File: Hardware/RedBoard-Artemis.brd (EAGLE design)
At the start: 68.6 x 58.4 mm, 115 parts, among them IC3 LM1117, J2 CORTEX_DEBUG, J3 POWER_JACKTOE, J5 USB-C, Q1 2.5A/30V/105mΩ, U1 ARTEMIS_MODULESMD, U3 AP2112-3.3V, U5 CH340C, Y1 32.768kHz

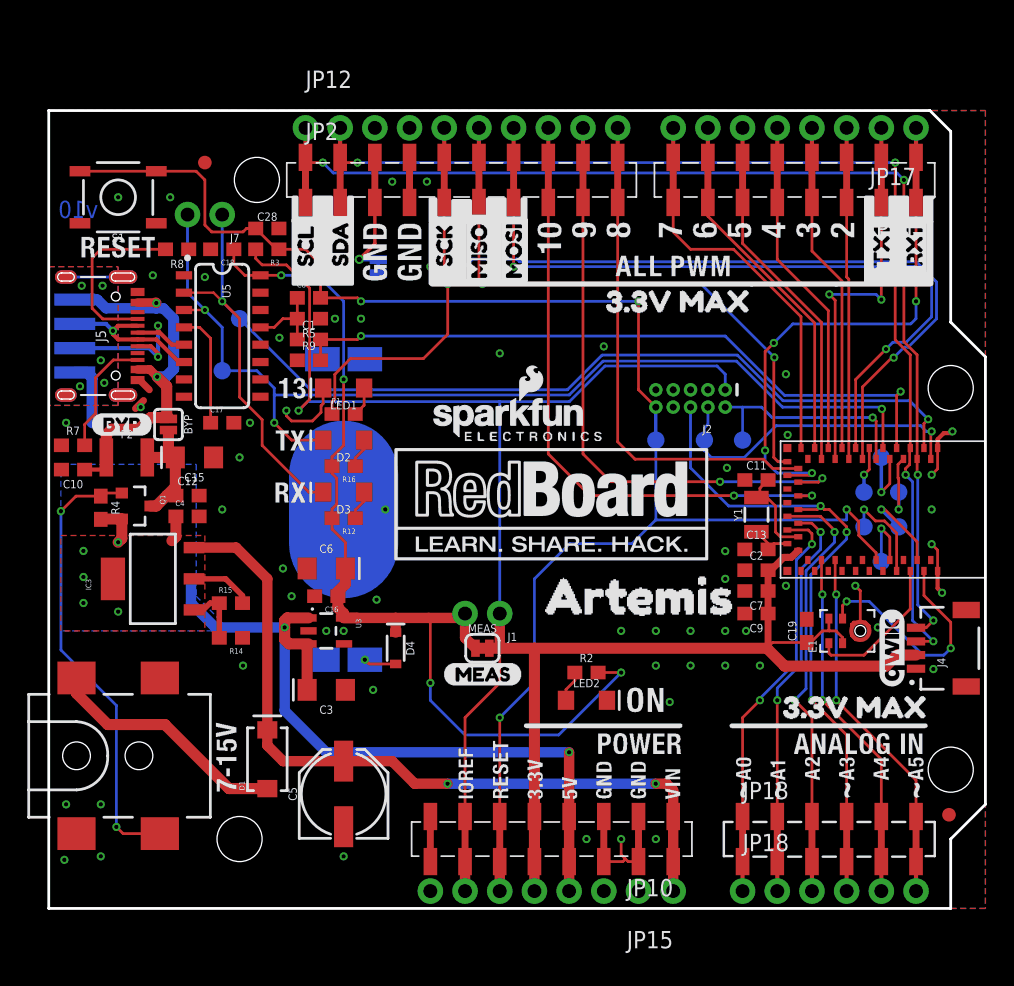
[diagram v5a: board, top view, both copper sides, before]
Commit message: Add bottom silk indicators. Move MEAS jumper.
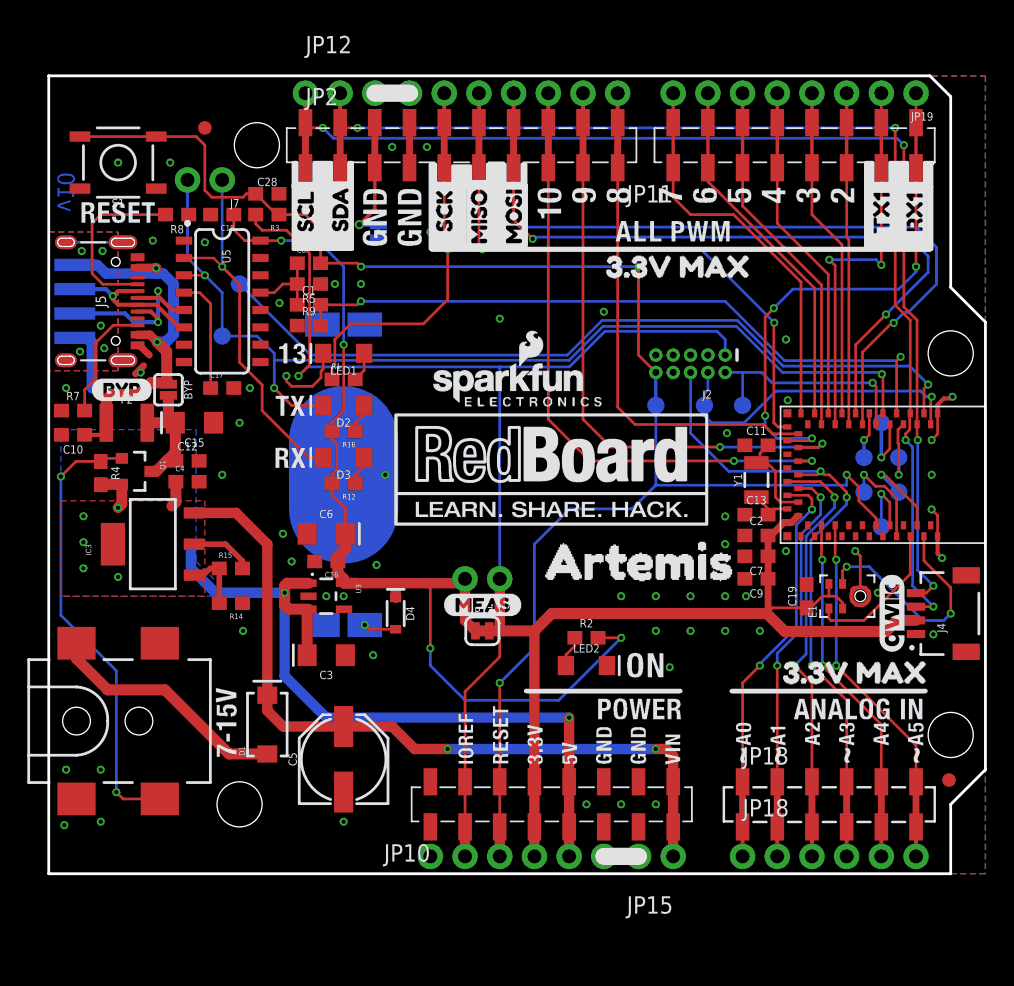
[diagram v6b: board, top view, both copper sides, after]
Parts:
- removed FRAME1: FRAME-LETTER, SparkFun-Aesthetics:CREATIVE_COMMONS
- removed MEAS: (no value), SparkFun-Jumpers:SMT-JUMPER_2_NC_TRACE_SILK
- added FRAME3: FRAME-LEDGER, SparkFun-Aesthetics:CREATIVE_COMMONS
- added JP19: (no value), SparkFun-Connectors:1X08_NO_SILK
- added U$1: (no value), buzzard_labels (6):SCL1
- added U$26: (no value), buzzard_labels (8):SCK9
- added U$27: (no value), buzzard_labels (8):MISO8
- added U$28: (no value), buzzard_labels (8):MOSI7
- added U$29: (no value), buzzard_labels (2):TX10
- added U$3: (no value), buzzard_labels (6):SDA0
- added U$30: (no value), buzzard_labels (2):RX11
- JP10, JP11: device SparkFun-Connectors:1X08_SMD_COMBINED -> SparkFun-Connectors:1X08_SMD_COMBINED_NC
- JP15: device SparkFun-Connectors:1X08_NO_SILK -> SparkFun-Connectors:1X08_NO_SILK@1
- JP17: value JP11 -> MEAS; device SparkFun-Connectors:1X08_NO_SILK -> SparkFun-Jumpers:SMT-JUMPER_2_NC_TRACE_SILK
- U1: device Testing:ARTEMIS_FP -> SparkFun-IC-Microcontroller:ARTEMIS_FP
- moved JP17 48.6 mm to (31.8, 17.8), turned to 0 degrees
- moved JP11 18.0 mm to (45.7, 53.3)
- moved JP10 18.0 mm to (27.9, 5.08)
- moved U$70 5.08 mm to (28.8, 19.7)
- moved JP2 2.54 mm to (18.8, 53.3)
- moved JP6 2.54 mm to (15.2, 53.3)
- moved U$20 2.54 mm to (26.9, 49.3)
- moved U$67 2.54 mm to (39.4, 44.5)
- moved C13 2.54 mm to (51.8, 26.3)
- moved C15 2.54 mm to (10.7, 33.0)
- moved C4 2.54 mm to (10.2, 28.7)
- moved F2 2.54 mm to (5.71, 33.0)
- moved R14 2.54 mm to (13.3, 19.8)
- moved TP11 2.54 mm to (62.2, 27.9)
- moved TP14 2.54 mm to (61.0, 33.0)
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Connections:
- net !RESET: now also JP10.6, JP10.6@2; no longer JP10.6A, JP10.6B
- net 3.3V: now also JP17.1; no longer MEAS.1
- net 5V: now also JP10.4, JP10.4@2; no longer JP10.4A, JP10.4B
- net GND: now also JP10.2, JP10.2@2, JP10.3, JP10.3@2; no longer JP10.2A, JP10.2B, JP10.3A, JP10.3B
- net VDD: now also JP10.5, JP10.5@2, JP10.7, JP10.7@2, JP17.2; no longer JP10.5A, JP10.5B, JP10.7A, JP10.7B, MEAS.2
- net VIN: now also JP10.1, JP10.1@2; no longer JP10.1A, JP10.1B
- net ~D0/RXI-1: now also JP11.1, JP11.1@2, JP19.1; no longer JP11.1A, JP11.1B, JP17.1
- net ~D1/TXO-1: now also JP11.2, JP11.2@2, JP19.2; no longer JP11.2A, JP11.2B, JP17.2
- net ~D2/A6: now also JP11.3, JP11.3@2, JP19.3; no longer JP11.3A, JP11.3B, JP17.3
- net ~D3: now also JP11.4, JP11.4@2, JP19.4; no longer JP11.4A, JP11.4B, JP17.4
- net ~D4: now also JP11.5, JP11.5@2, JP19.5; no longer JP11.5A, JP11.5B, JP17.5
- net ~D5: now also JP11.6, JP11.6@2, JP19.6; no longer JP11.6A, JP11.6B, JP17.6
- net ~D6: now also JP11.7, JP11.7@2, JP19.7; no longer JP11.7A, JP11.7B, JP17.7
- net ~D7: now also JP11.8, JP11.8@2, JP19.8; no longer JP11.8A, JP11.8B, JP17.8
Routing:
- net GND: track 30.3 -> 26.0 mm
- net VDD: track 155.1 -> 151.0 mm
- net ~D11/MOSI: track 56.2 -> 54.5 mm
- net 3.3V: track 73.3 -> 74.5 mm
- net ~D0/RXI-1: track 39.7 -> 39.2 mm
